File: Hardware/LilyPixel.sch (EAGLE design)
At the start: 11 parts, among them U1 WS2811

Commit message: Update to v10 for release
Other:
- note added: "10"
- note removed: "01"
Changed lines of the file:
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@@
 <text x="81.28" y="111.76" size="5.08" layer="91">+</text>
 <text x="81.28" y="99.06" size="5.08" layer="91">-</text>
-<text x="237.998" y="6.858" size="3.81" layer="94">01</text>
+<text x="237.998" y="6.858" size="3.81" layer="94">10</text>
 <text x="154.94" y="111.76" size="3.81" layer="94">DI</text>
 <text x="154.94" y="101.6" size="3.81" layer="94">DO</text>

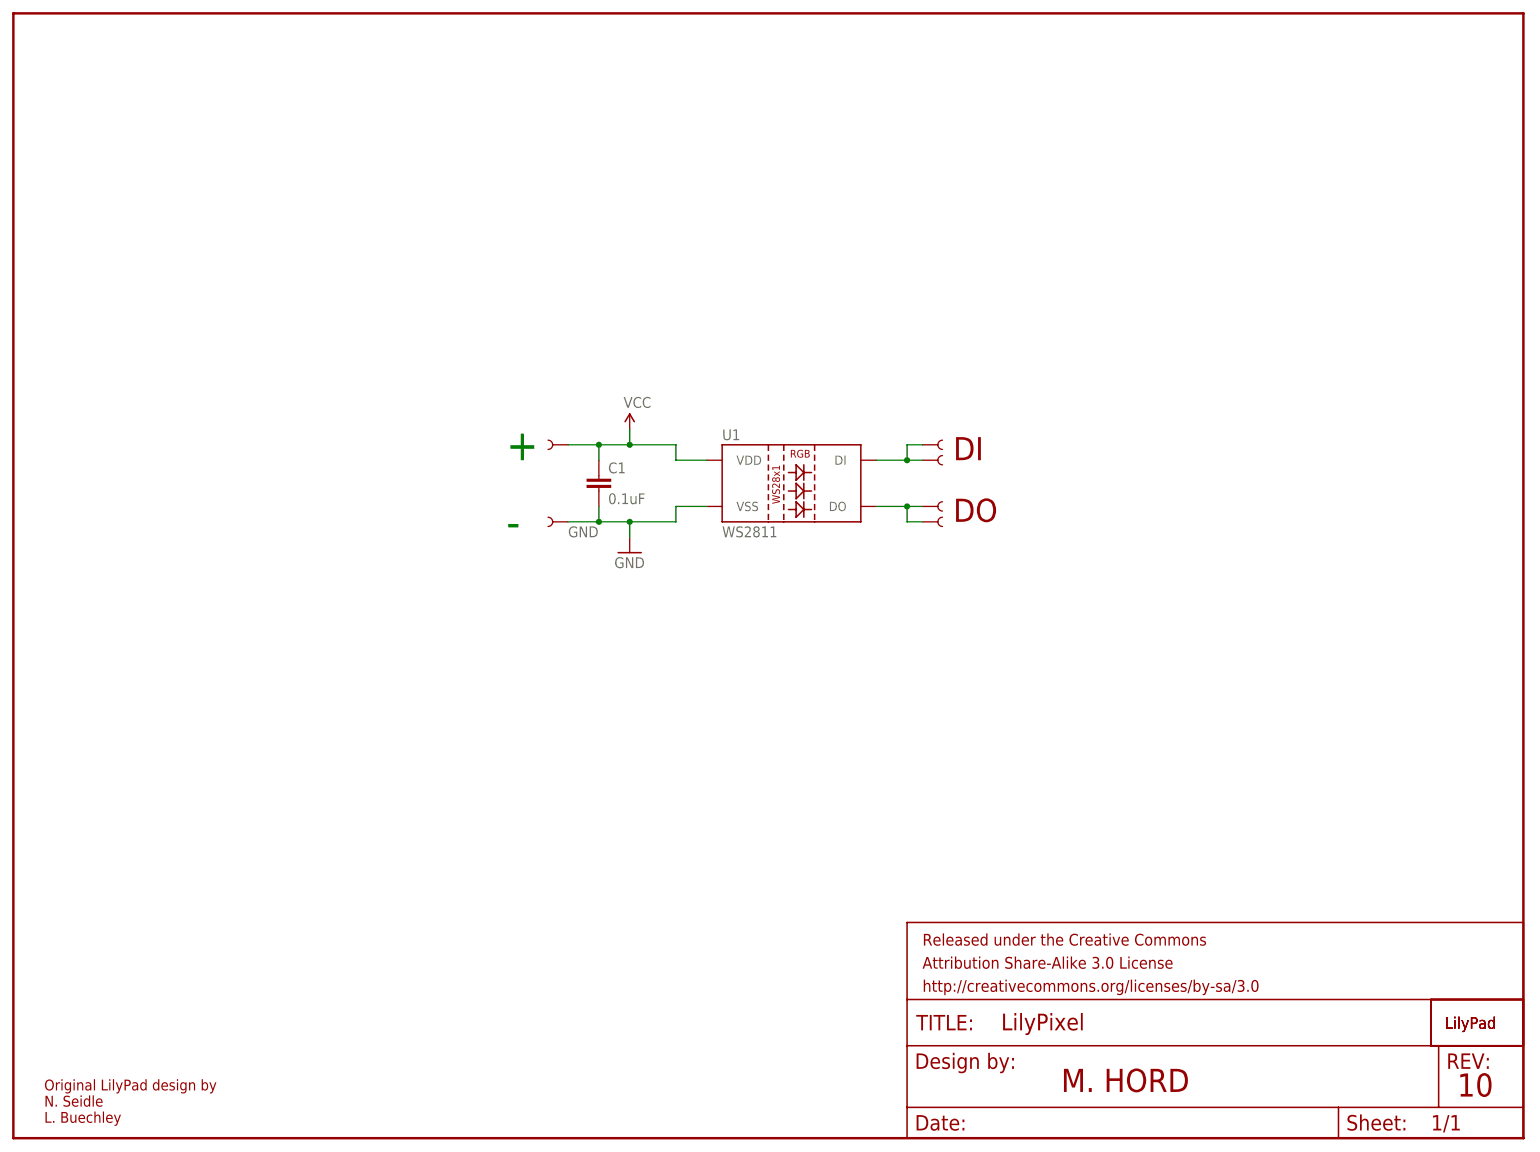
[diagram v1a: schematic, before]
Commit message: replaced led package
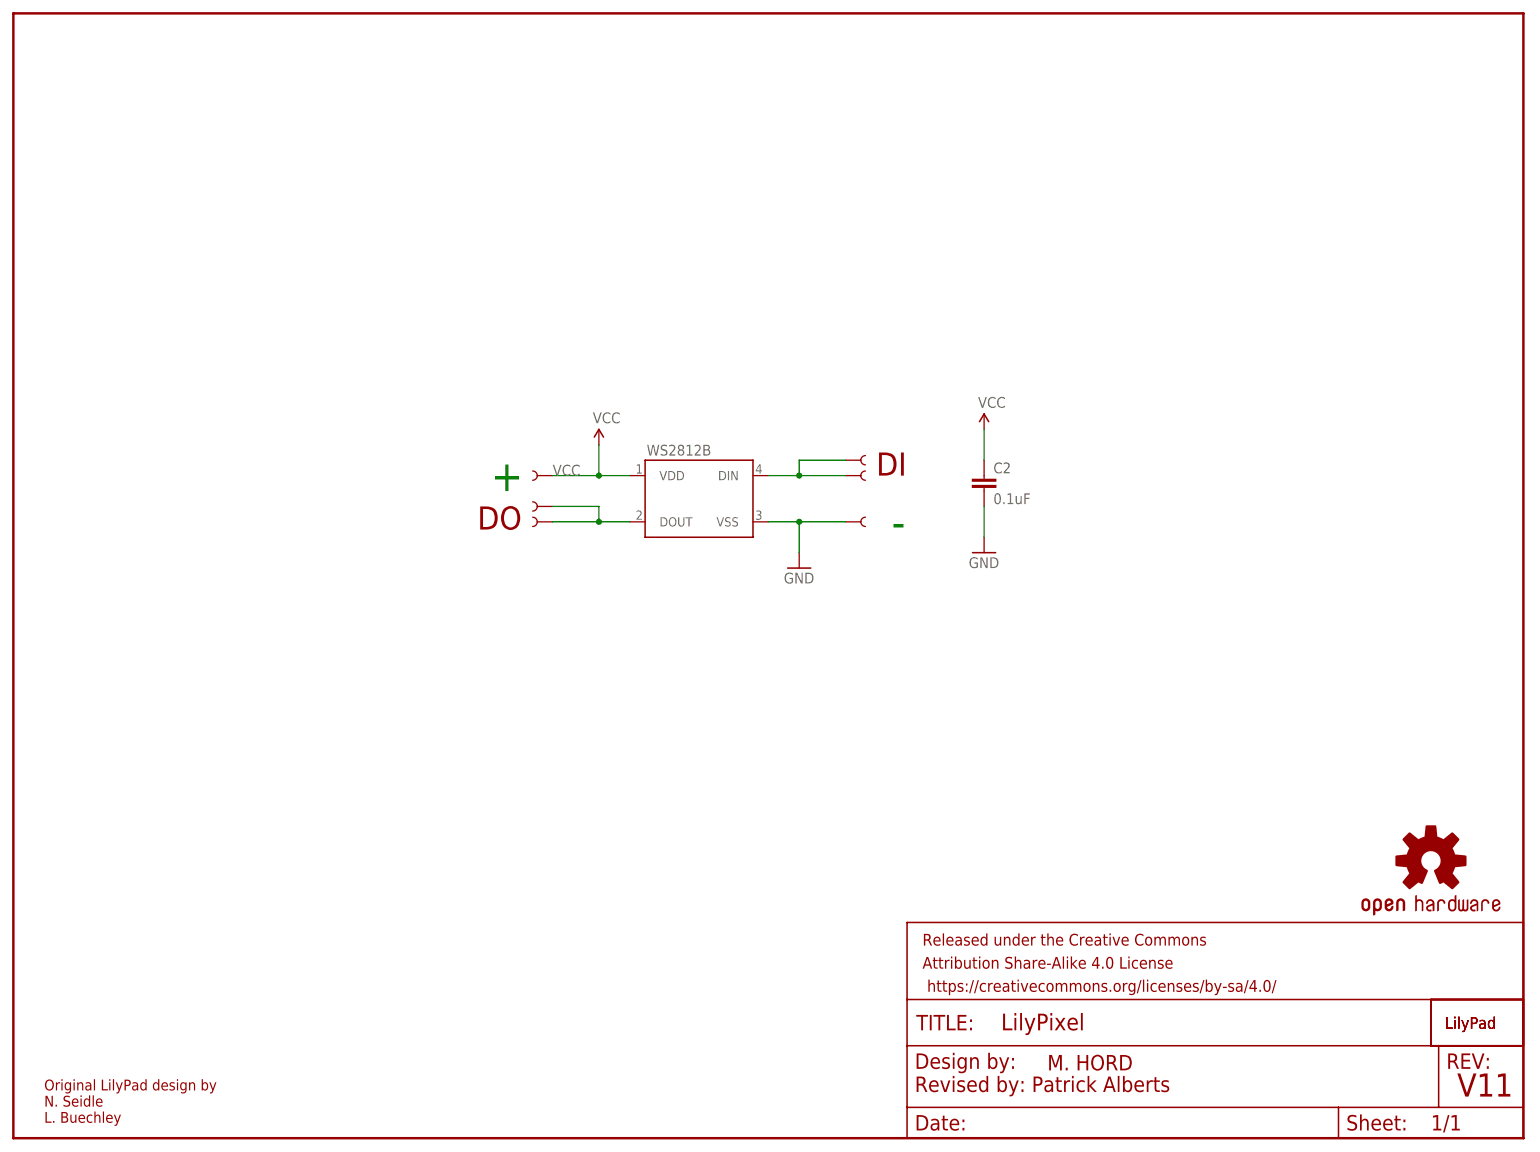
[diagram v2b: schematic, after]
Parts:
- removed C1: 0.1uF, SparkFun-Capacitors:0.1UF-25V(+80/-20%)(0603)
- removed U$2, U$3, U$4, U$5, U$6, U$7: SEWTAP6, LilyPad-Wearables:SEWTAP6
- removed U1: WS2811, SparkFun-LED:LED-TRICOLOR-5050-ICWS2811
- added C2: 0.1uF, SparkFun-Capacitors:0.1UF-25V(+80/-20%)(0603)
- added LOGO1: OSHW-LOGOS, SparkFun-Aesthetics:OSHW-LOGOS
- added U$10, U$11, U$12, U$13, U$14, U$9: SEWTAP6, LilyPad-Wearables:SEWTAP6
- added WS2812B: (no value), SparkFun-LED:WS2812B
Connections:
- removed net DI: U$2.1, U$4.1, U1.DI
- removed net DO: U$3.1, U$5.1, U1.DO
- new net DI1: U$10.1, U$9.1, WS2812B.DIN
- new net DO1: U$11.1, U$12.1, WS2812B.DOUT
- net GND: now also C2.2, U$14.1, WS2812B.VSS; no longer C1.2, U$7.1, U1.VSS
- net VCC: now also C2.1, U$13.1, WS2812B.VDD; no longer C1.1, U$6.1, U1.VDD
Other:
- note added: "Revised by: Patrick Alberts"
- note added: "V11"
- note removed: "10"

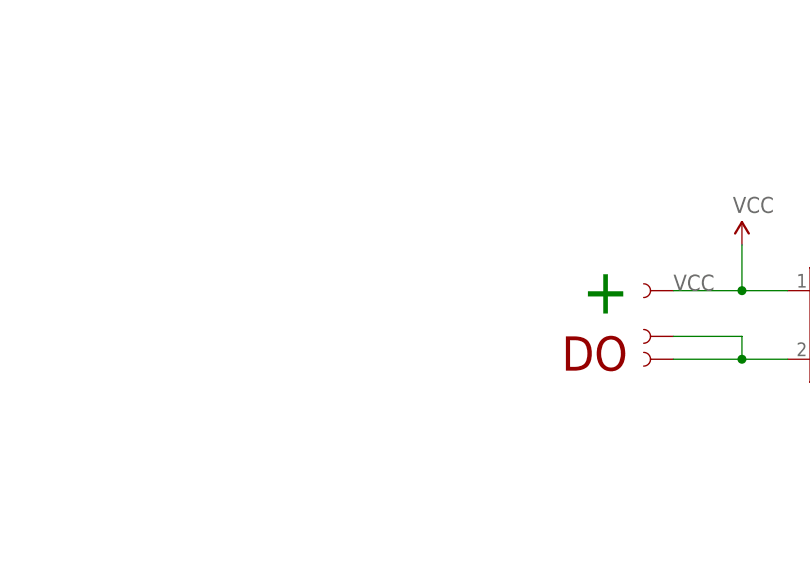
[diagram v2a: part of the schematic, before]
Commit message: LED/Silk Orientation
Fixed the orientation of the silk, LED and petals.

Added Sparkfun Flame
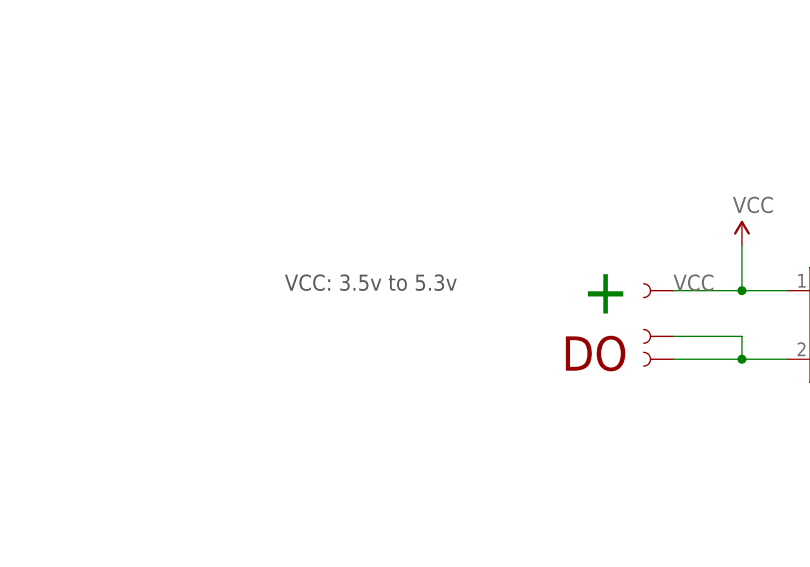
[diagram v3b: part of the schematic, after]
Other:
- note added: "VCC: 3.5v to 5.3v"
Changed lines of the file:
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@@
 <text x="144.78" y="99.06" size="5.08" layer="91">-</text>
 <text x="148.59" y="7.62" size="2.54" layer="94">Revised by: Patrick Alberts</text>
+<text x="45.72" y="109.22" size="1.778" layer="97">VCC: 3.5v to 5.3v</text>
 </plain>
 <instances>

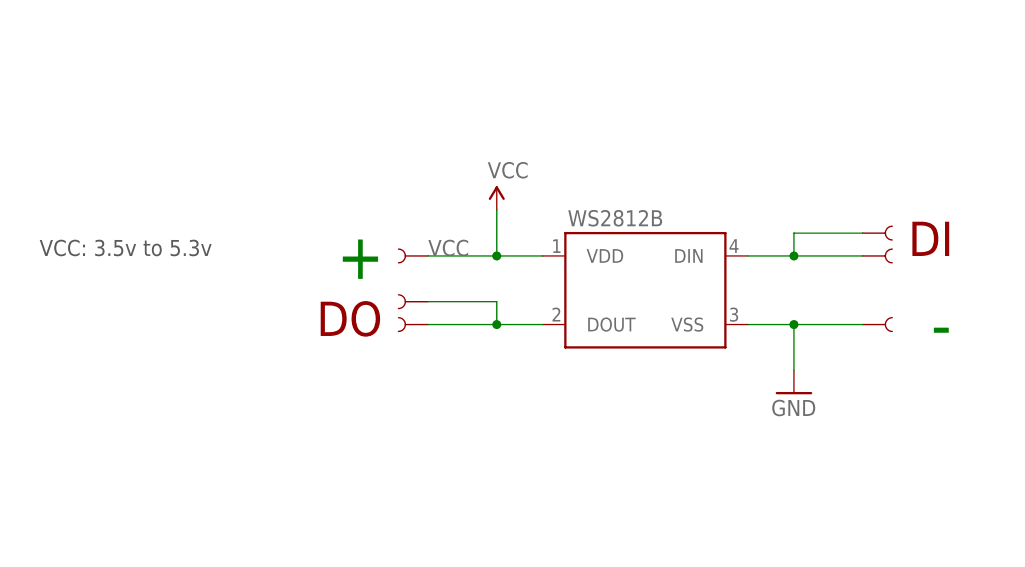
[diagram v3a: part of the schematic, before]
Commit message: Re assigned Petals, full complete re route.
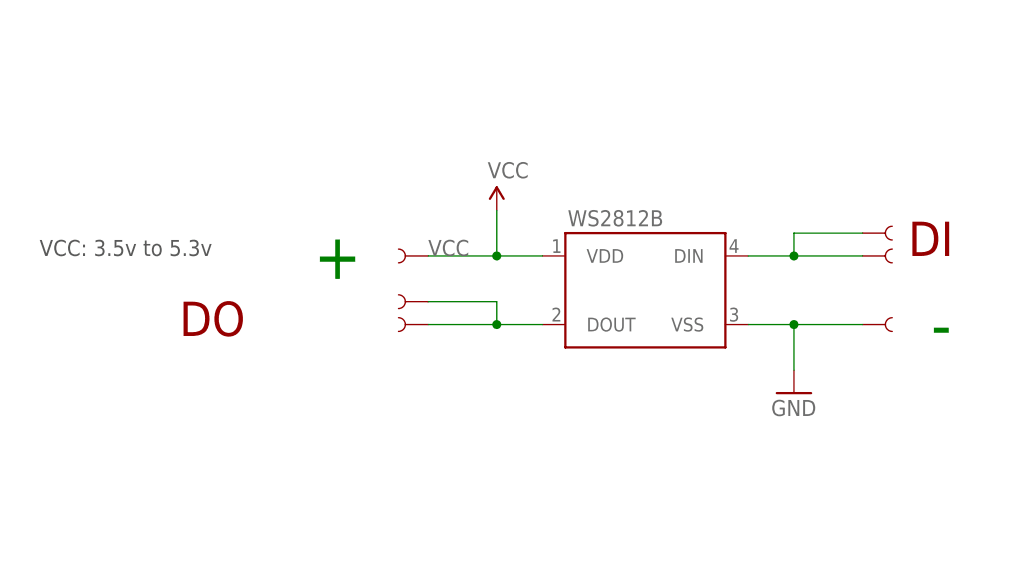
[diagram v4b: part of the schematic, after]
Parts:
- renumbered U$10 to JP5, U$11 to JP1, U$12 to JP2, U$13 to JP4, U$14 to JP3, U$9 to JP6
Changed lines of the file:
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@@
 <part name="U$1" library="LilyPad-Wearables" deviceset="LOGO-LP" device="LP"/>
 <part name="WS2812B" library="SparkFun-LED" deviceset="WS2812B" device=""/>
-<part name="U$9" library="LilyPad-Wearables" deviceset="SEWTAP" device="6"/>
-<part name="U$10" library="LilyPad-Wearables" deviceset="SEWTAP" device="6"/>
-<part name="U$11" library="LilyPad-Wearables" deviceset="SEWTAP" device="6"/>
-<part name="U$12" library="LilyPad-Wearables" deviceset="SEWTAP" device="6"/>
+<part name="JP4" library="LilyPad-Wearables" deviceset="SEWTAP" device="6"/>
+<part name="JP5" library="LilyPad-Wearables" deviceset="SEWTAP" device="6"/>
+<part name="JP3" library="LilyPad-Wearables" deviceset="SEWTAP" device="6"/>
+<part name="JP2" library="LilyPad-Wearables" deviceset="SEWTAP" device="6"/>
 <part name="P+2" library="SparkFun" deviceset="VCC" device=""/>
-<part name="U$13" library="LilyPad-Wearables" deviceset="SEWTAP" device="6"/>
+<part name="JP1" library="LilyPad-Wearables" deviceset="SEWTAP" device="6"/>
 <part name="C2" library="SparkFun-Capacitors" deviceset="0.1UF-25V(+80/-20%)(0603)" device="" value="0.1uF"/>
 <part name="GND2" library="SparkFun" deviceset="GND" device=""/>
-<part name="U$14" library="LilyPad-Wearables" deviceset="SEWTAP" device="6"/>
+<part name="JP6" library="LilyPad-Wearables" deviceset="SEWTAP" device="6"/>
 <part name="P+3" library="SparkFun" deviceset="VCC" device=""/>
 <part name="GND3" library="SparkFun" deviceset="GND" device=""/>
@@
 L. Buechley</text>
 <text x="142.24" y="109.22" size="3.81" layer="94">DI</text>
-<text x="83.82" y="104.14" size="3.81" layer="94" rot="R180">DO</text>
-<text x="78.74" y="106.68" size="5.08" layer="91">+</text>
+<text x="68.58" y="104.14" size="3.81" layer="94" rot="R180">DO</text>
+<text x="76.2" y="106.68" size="5.08" layer="91">+</text>
 <text x="144.78" y="99.06" size="5.08" layer="91">-</text>
 <text x="148.59" y="7.62" size="2.54" layer="94">Revised by: Patrick Alberts</text>
@@
 <instance part="U$1" gate="G$1" x="236.22" y="17.78"/>
 <instance part="WS2812B" gate="G$1" x="106.68" y="104.14"/>
-<instance part="U$9" gate="G$1" x="139.7" y="111.76"/>
-<instance part="U$10" gate="G$1" x="139.7" y="109.22"/>
-<instance part="U$11" gate="G$1" x="86.36" y="101.6" rot="R180"/>
-<instance part="U$12" gate="G$1" x="86.36" y="104.14" rot="R180"/>
+<instance part="JP4" gate="G$1" x="86.36" y="109.22" rot="R180"/>
+<instance part="JP5" gate="G$1" x="139.7" y="109.22"/>
+<instance part="JP3" gate="G$1" x="139.7" y="101.6"/>
+<instance part="JP2" gate="G$1" x="86.36" y="104.14" rot="R180"/>
 <instance part="P+2" gate="1" x="96.52" y="114.3"/>
-<instance part="U$13" gate="G$1" x="86.36" y="109.22" rot="R180"/>
+<instance part="JP1" gate="G$1" x="86.36" y="101.6" rot="R180"/>
 <instance part="C2" gate="G$1" x="160.02" y="106.68"/>
 <instance part="GND2" gate="1" x="129.54" y="93.98"/>
-<instance part="U$14" gate="G$1" x="139.7" y="101.6"/>
+<instance part="JP6" gate="G$1" x="139.7" y="111.76"/>
 <instance part="P+3" gate="1" x="160.02" y="116.84"/>
 <instance part="GND3" gate="1" x="160.02" y="96.52"/>
@@
 <segment>
 <wire x1="96.52" y1="109.22" x2="96.52" y2="114.3" width="0.1524" layer="91"/>
-<junction x="96.52" y="109.22"/>
 <pinref part="P+2" gate="1" pin="VCC"/>
 <wire x1="96.52" y1="109.22" x2="101.6" y2="109.22" width="0.1524" layer="91"/>
 <label x="88.9" y="109.22" size="1.778" layer="95"/>
-<pinref part="U$13" gate="G$1" pin="1"/>
-<wire x1="96.52" y1="109.22" x2="88.9" y2="109.22" width="0.1524" layer="91"/>
 <pinref part="WS2812B" gate="G$1" pin="VDD"/>
+<pinref part="JP4" gate="G$1" pin="1"/>
+<wire x1="88.9" y1="109.22" x2="96.52" y2="109.22" width="0.1524" layer="91"/>
+<junction x="96.52" y="109.22"/>
 </segment>
 <segment>
@@
 <wire x1="129.54" y1="101.6" x2="129.54" y2="96.52" width="0.1524" layer="91"/>
 <pinref part="GND2" gate="1" pin="GND"/>
-<wire x1="129.54" y1="101.6" x2="137.16" y2="101.6" width="0.1524" layer="91"/>
+<pinref part="JP3" gate="G$1" pin="1"/>
+<wire x1="137.16" y1="101.6" x2="129.54" y2="101.6" width="0.1524" layer="91"/>
 <junction x="129.54" y="101.6"/>
-<pinref part="U$14" gate="G$1" pin="1"/>
 </segment>
 </net>
@@
 <wire x1="129.54" y1="109.22" x2="124.46" y2="109.22" width="0.1524" layer="91"/>
 <wire x1="129.54" y1="111.76" x2="129.54" y2="109.22" width="0.1524" layer="91"/>
-<pinref part="U$9" gate="G$1" pin="1"/>
-<wire x1="129.54" y1="111.76" x2="137.16" y2="111.76" width="0.1524" layer="91"/>
-<pinref part="U$10" gate="G$1" pin="1"/>
+<pinref part="JP5" gate="G$1" pin="1"/>
 <wire x1="137.16" y1="109.22" x2="129.54" y2="109.22" width="0.1524" layer="91"/>
 <junction x="129.54" y="109.22"/>
 <pinref part="WS2812B" gate="G$1" pin="DIN"/>
+<pinref part="JP6" gate="G$1" pin="1"/>
+<wire x1="137.16" y1="111.76" x2="129.54" y2="111.76" width="0.1524" layer="91"/>
 </segment>
 </net>
@@
 <wire x1="96.52" y1="101.6" x2="101.6" y2="101.6" width="0.1524" layer="91"/>
 <wire x1="96.52" y1="104.14" x2="96.52" y2="101.6" width="0.1524" layer="91"/>
-<pinref part="U$12" gate="G$1" pin="1"/>
+<pinref part="JP2" gate="G$1" pin="1"/>
 <wire x1="88.9" y1="104.14" x2="96.52" y2="104.14" width="0.1524" layer="91"/>
-<pinref part="U$11" gate="G$1" pin="1"/>
+<pinref part="WS2812B" gate="G$1" pin="DOUT"/>
+<pinref part="JP1" gate="G$1" pin="1"/>
 <wire x1="88.9" y1="101.6" x2="96.52" y2="101.6" width="0.1524" layer="91"/>
 <junction x="96.52" y="101.6"/>
-<pinref part="WS2812B" gate="G$1" pin="DOUT"/>
 </segment>
 </net>
